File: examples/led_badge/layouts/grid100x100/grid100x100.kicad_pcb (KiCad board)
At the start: 4 copper layers, 200 parts

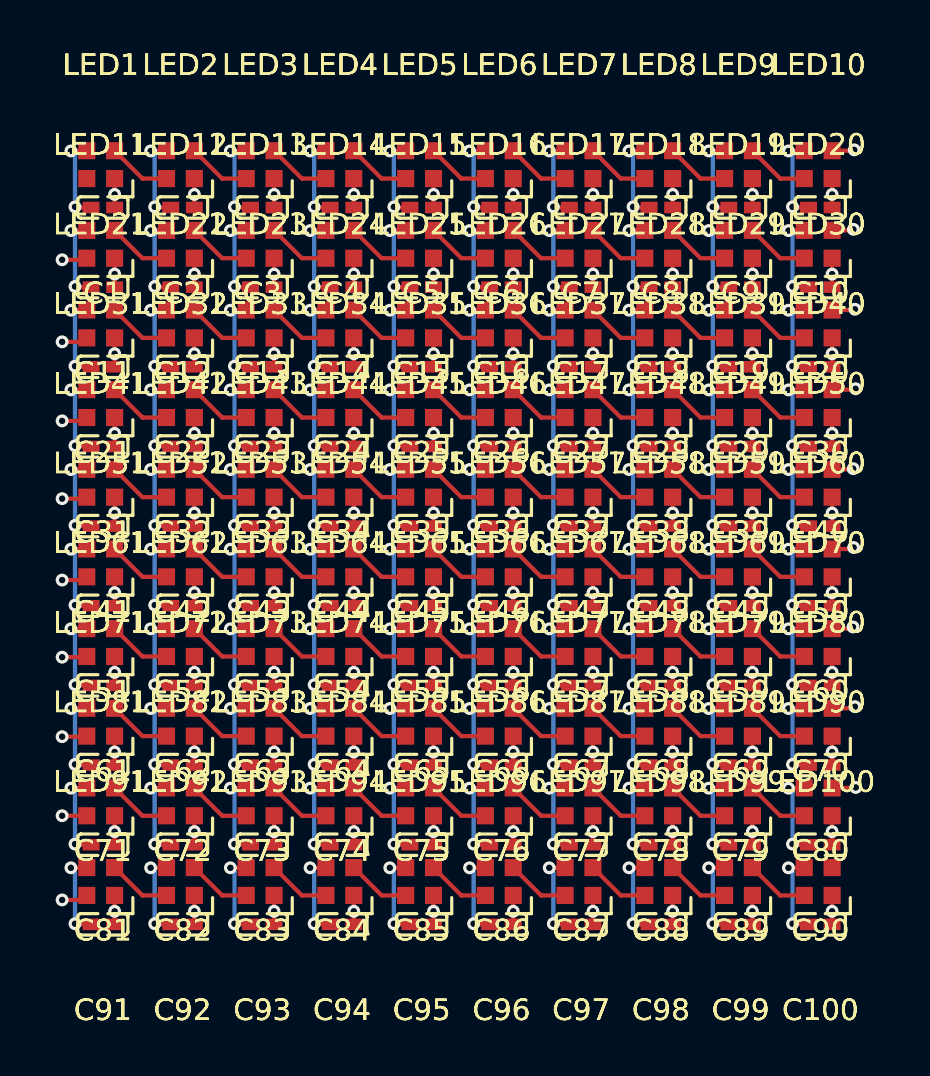
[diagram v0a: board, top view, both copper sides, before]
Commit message: fix 3d models
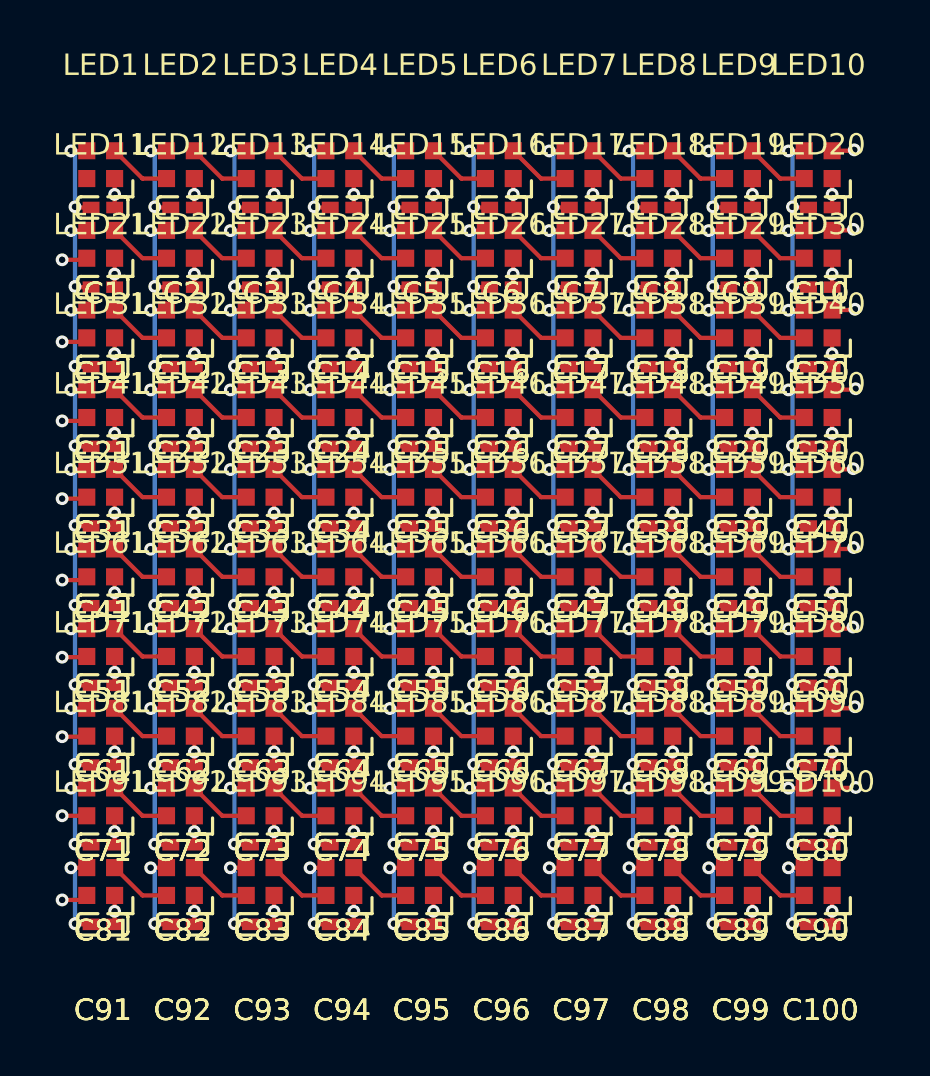
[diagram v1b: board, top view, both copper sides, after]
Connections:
- net line renamed -line-0
- net line-1 renamed -line-1
- net line-10 renamed -line-10
- net line-2 renamed -line-2
- net line-3 renamed -line-3
- net line-4 renamed -line-4
- net line-5 renamed -line-5
- net line-6 renamed -line-6
- net line-7 renamed -line-7
- net line-8 renamed -line-8
- net line-9 renamed -line-9
- net rows[0]-DOUT renamed rows[0]-DOUT-0
- net rows[1]-DOUT renamed rows[1]-DOUT-0
- net rows[2]-DOUT renamed rows[2]-DOUT-0
- net rows[3]-DOUT renamed rows[3]-DOUT-0
- net rows[4]-DOUT renamed rows[4]-DOUT-0
- net rows[5]-DOUT renamed rows[5]-DOUT-0
- net rows[6]-DOUT renamed rows[6]-DOUT-0
- net rows[7]-DOUT renamed rows[7]-DOUT-0
- net rows[8]-DOUT renamed rows[8]-DOUT-0
- net rows[9]-DOUT renamed rows[9]-DOUT-0

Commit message: almost complete layout
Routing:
- net hv: track 135.0 -> 173.8 mm

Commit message: just need usb to work
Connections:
- net -line-0 renamed rows[0]-data_in-line
- net -line-1 renamed data_out-line
- net -line-10 renamed rows[9]-data_in-line
- net -line-2 renamed rows[1]-data_in-line
- net -line-3 renamed rows[2]-data_in-line
- net -line-4 renamed rows[3]-data_in-line
- net -line-5 renamed rows[4]-data_in-line
- net -line-6 renamed rows[5]-data_in-line
- net -line-7 renamed rows[6]-data_in-line
- net -line-8 renamed rows[7]-data_in-line
- net -line-9 renamed rows[8]-data_in-line
- net gnd renamed GND
- net hv renamed VCC
- net rows[0]-DOUT-0 renamed leds[1]-data_in-DIN-0
- net rows[0]-DOUT-1 renamed leds[2]-data_in-DIN-0
- net rows[0]-DOUT-2 renamed leds[3]-data_in-DIN-0
- net rows[0]-DOUT-3 renamed leds[4]-data_in-DIN-0
- net rows[0]-DOUT-4 renamed leds[5]-data_in-DIN-0
- net rows[0]-DOUT-5 renamed leds[6]-data_in-DIN-0
- net rows[0]-DOUT-6 renamed leds[7]-data_in-DIN-0
- net rows[0]-DOUT-7 renamed leds[8]-data_in-DIN-0
- net rows[0]-DOUT-8 renamed leds[9]-data_in-DIN-0
- net rows[1]-DOUT-0 renamed leds[1]-data_in-DIN-1
- net rows[1]-DOUT-1 renamed leds[2]-data_in-DIN-1
- net rows[1]-DOUT-2 renamed leds[3]-data_in-DIN-1
- net rows[1]-DOUT-3 renamed leds[4]-data_in-DIN-1
- net rows[1]-DOUT-4 renamed leds[5]-data_in-DIN-1
- net rows[1]-DOUT-5 renamed leds[6]-data_in-DIN-1
- net rows[1]-DOUT-6 renamed leds[7]-data_in-DIN-1
- net rows[1]-DOUT-7 renamed leds[8]-data_in-DIN-1
- net rows[1]-DOUT-8 renamed leds[9]-data_in-DIN-1
- net rows[2]-DOUT-0 renamed leds[1]-data_in-DIN-2
- net rows[2]-DOUT-1 renamed leds[2]-data_in-DIN-2
- net rows[2]-DOUT-2 renamed leds[3]-data_in-DIN-2
- net rows[2]-DOUT-3 renamed leds[4]-data_in-DIN-2
- net rows[2]-DOUT-4 renamed leds[5]-data_in-DIN-2
- net rows[2]-DOUT-5 renamed leds[6]-data_in-DIN-2
- net rows[2]-DOUT-6 renamed leds[7]-data_in-DIN-2
- net rows[2]-DOUT-7 renamed leds[8]-data_in-DIN-2
- net rows[2]-DOUT-8 renamed leds[9]-data_in-DIN-2
- net rows[3]-DOUT-0 renamed leds[1]-data_in-DIN-3
- net rows[3]-DOUT-1 renamed leds[2]-data_in-DIN-3
- net rows[3]-DOUT-2 renamed leds[3]-data_in-DIN-3
- net rows[3]-DOUT-3 renamed leds[4]-data_in-DIN-3
- net rows[3]-DOUT-4 renamed leds[5]-data_in-DIN-3
- net rows[3]-DOUT-5 renamed leds[6]-data_in-DIN-3
- net rows[3]-DOUT-6 renamed leds[7]-data_in-DIN-3
- net rows[3]-DOUT-7 renamed leds[8]-data_in-DIN-3
- net rows[3]-DOUT-8 renamed leds[9]-data_in-DIN-3
- net rows[4]-DOUT-0 renamed leds[1]-data_in-DIN-4
- net rows[4]-DOUT-1 renamed leds[2]-data_in-DIN-4
- net rows[4]-DOUT-2 renamed leds[3]-data_in-DIN-4
- net rows[4]-DOUT-3 renamed leds[4]-data_in-DIN-4
- net rows[4]-DOUT-4 renamed leds[5]-data_in-DIN-4
- net rows[4]-DOUT-5 renamed leds[6]-data_in-DIN-4
- net rows[4]-DOUT-6 renamed leds[7]-data_in-DIN-4
- net rows[4]-DOUT-7 renamed leds[8]-data_in-DIN-4
- net rows[4]-DOUT-8 renamed leds[9]-data_in-DIN-4
- net rows[5]-DOUT-0 renamed leds[1]-data_in-DIN-5
- net rows[5]-DOUT-1 renamed leds[2]-data_in-DIN-5
- net rows[5]-DOUT-2 renamed leds[3]-data_in-DIN-5
- net rows[5]-DOUT-3 renamed leds[4]-data_in-DIN-5
- net rows[5]-DOUT-4 renamed leds[5]-data_in-DIN-5
- net rows[5]-DOUT-5 renamed leds[6]-data_in-DIN-5
- net rows[5]-DOUT-6 renamed leds[7]-data_in-DIN-5
- net rows[5]-DOUT-7 renamed leds[8]-data_in-DIN-5
- net rows[5]-DOUT-8 renamed leds[9]-data_in-DIN-5
- net rows[6]-DOUT-0 renamed leds[1]-data_in-DIN-6
- net rows[6]-DOUT-1 renamed leds[2]-data_in-DIN-6
- net rows[6]-DOUT-2 renamed leds[3]-data_in-DIN-6
- net rows[6]-DOUT-3 renamed leds[4]-data_in-DIN-6
- net rows[6]-DOUT-4 renamed leds[5]-data_in-DIN-6
- net rows[6]-DOUT-5 renamed leds[6]-data_in-DIN-6
- net rows[6]-DOUT-6 renamed leds[7]-data_in-DIN-6
- net rows[6]-DOUT-7 renamed leds[8]-data_in-DIN-6
- net rows[6]-DOUT-8 renamed leds[9]-data_in-DIN-6
- net rows[7]-DOUT-0 renamed leds[1]-data_in-DIN-7
- net rows[7]-DOUT-1 renamed leds[2]-data_in-DIN-7
- net rows[7]-DOUT-2 renamed leds[3]-data_in-DIN-7
- net rows[7]-DOUT-3 renamed leds[4]-data_in-DIN-7
- net rows[7]-DOUT-4 renamed leds[5]-data_in-DIN-7
- net rows[7]-DOUT-5 renamed leds[6]-data_in-DIN-7
- net rows[7]-DOUT-6 renamed leds[7]-data_in-DIN-7
- net rows[7]-DOUT-7 renamed leds[8]-data_in-DIN-7
- net rows[7]-DOUT-8 renamed leds[9]-data_in-DIN-7
- net rows[8]-DOUT-0 renamed leds[1]-data_in-DIN-8
- net rows[8]-DOUT-1 renamed leds[2]-data_in-DIN-8
- net rows[8]-DOUT-2 renamed leds[3]-data_in-DIN-8
- net rows[8]-DOUT-3 renamed leds[4]-data_in-DIN-8
- net rows[8]-DOUT-4 renamed leds[5]-data_in-DIN-8
- net rows[8]-DOUT-5 renamed leds[6]-data_in-DIN-8
- net rows[8]-DOUT-6 renamed leds[7]-data_in-DIN-8
- net rows[8]-DOUT-7 renamed leds[8]-data_in-DIN-8
- net rows[8]-DOUT-8 renamed leds[9]-data_in-DIN-8
- net rows[9]-DOUT-0 renamed leds[1]-data_in-DIN-9
- net rows[9]-DOUT-1 renamed leds[2]-data_in-DIN-9
- net rows[9]-DOUT-2 renamed leds[3]-data_in-DIN-9
- net rows[9]-DOUT-3 renamed leds[4]-data_in-DIN-9
- net rows[9]-DOUT-4 renamed leds[5]-data_in-DIN-9
- net rows[9]-DOUT-5 renamed leds[6]-data_in-DIN-9
- net rows[9]-DOUT-6 renamed leds[7]-data_in-DIN-9
- net rows[9]-DOUT-7 renamed leds[8]-data_in-DIN-9
- net rows[9]-DOUT-8 renamed leds[9]-data_in-DIN-9
